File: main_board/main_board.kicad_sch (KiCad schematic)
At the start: 65 parts, among them J1 USB_B_Micro, J2 Conn_ARM_JTAG_SWD_10, Q1 NX3008PBK,215, Q2 T2N7002AK,LM, Q3 NX3008PBK,215, U1 SSD1306, U2 ESP32-S2-SOLO, U3 TLV62568PDRLT, U4 MCP73832, U7 MAX17055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

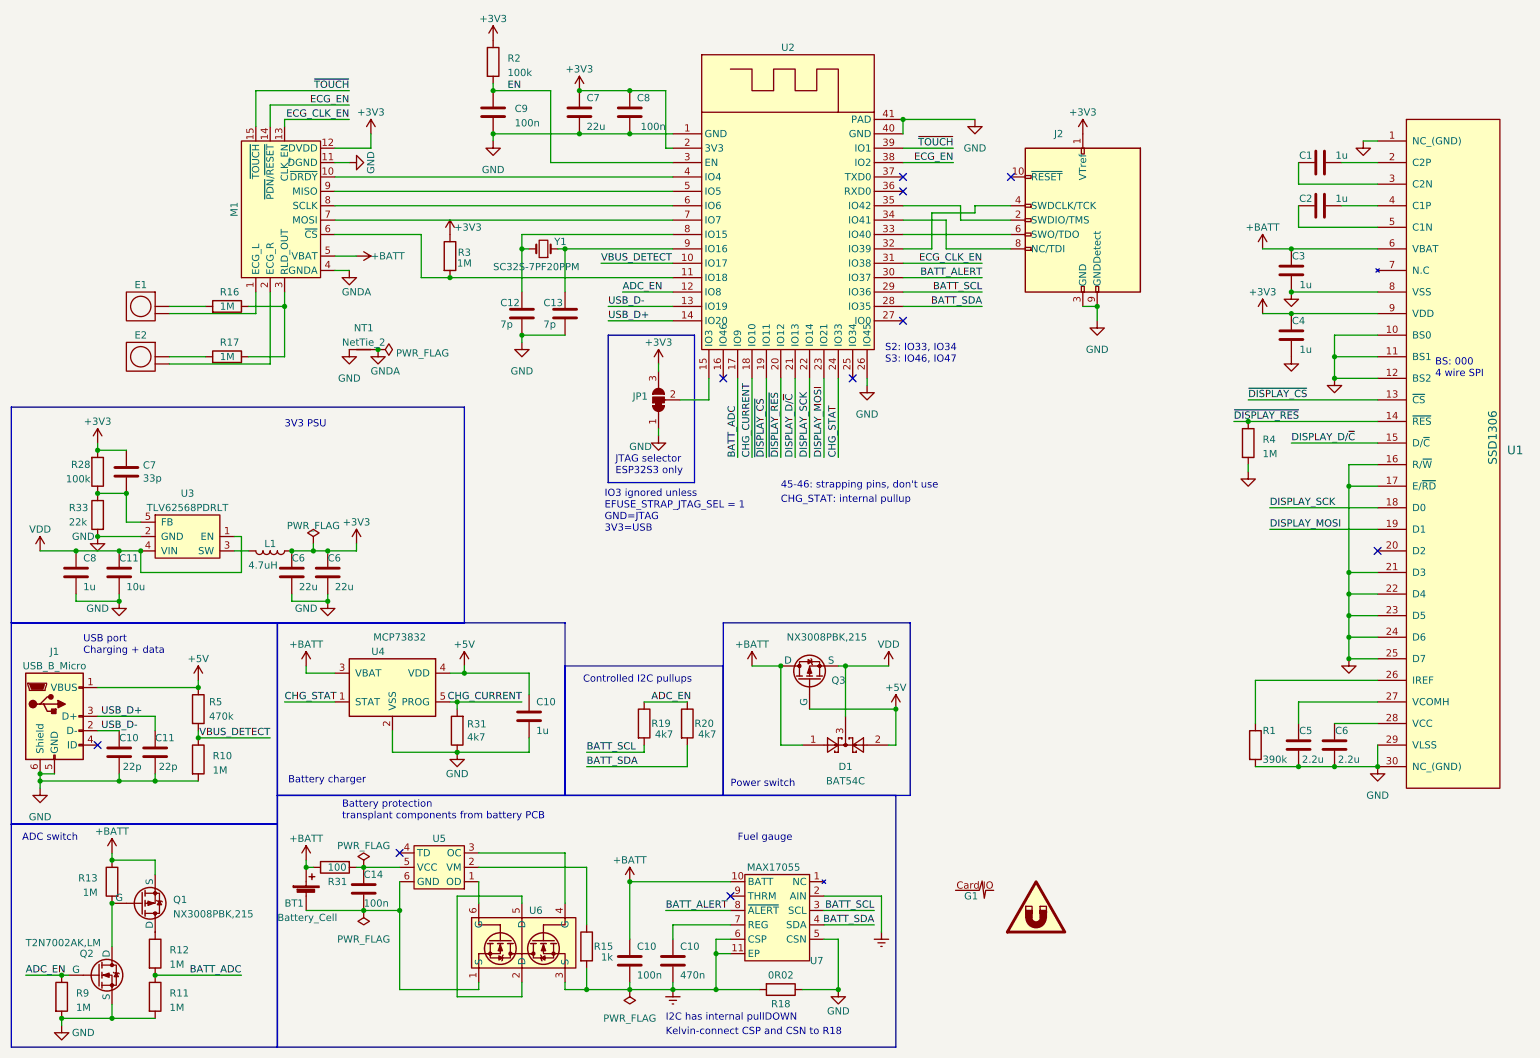
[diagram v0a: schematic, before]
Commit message: Remove battery ADC parts, simplify and tweak routing, add locking holes to jtag
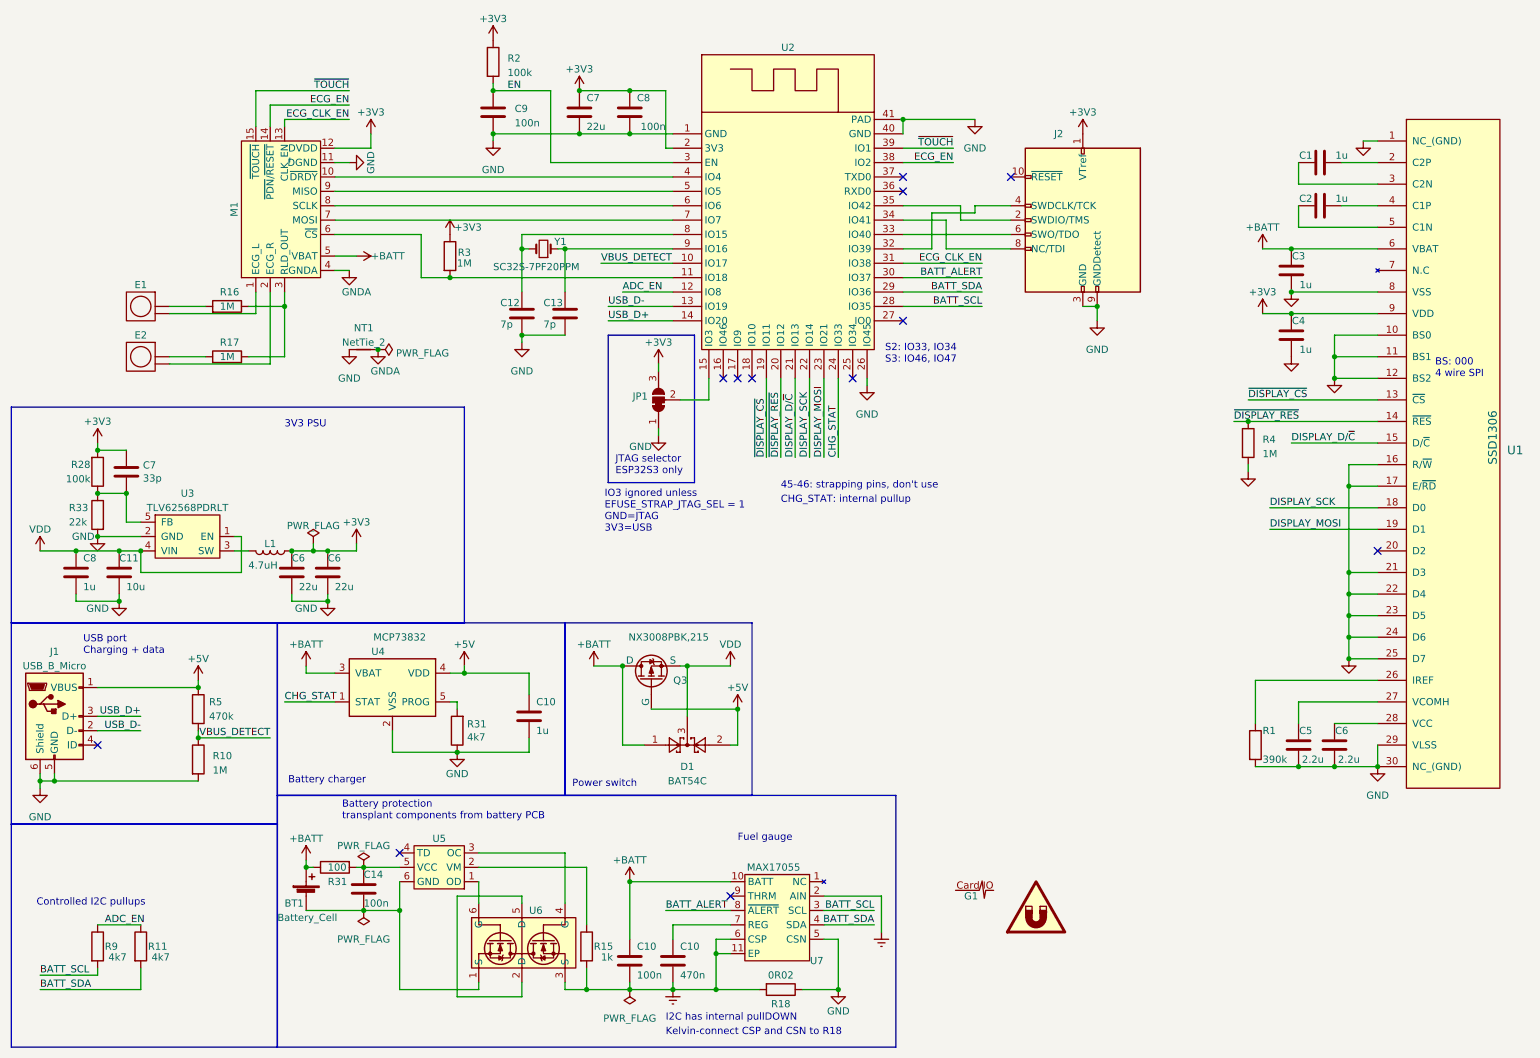
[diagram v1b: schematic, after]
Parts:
- removed C10, C11: 22p, Capacitor_SMD:C_0603_1608Metric, symbol Device:C
- removed Q1: NX3008PBK,215, Package_TO_SOT_SMD:SOT-23, symbol main_board_parts:PMOS
- removed Q2: T2N7002AK,LM, Package_TO_SOT_SMD:SOT-23, symbol main_board_parts:NMOS
- removed R12, R13: 1M, Resistor_SMD:R_0603_1608Metric, symbol Device:R
- removed R19, R20: 4k7, Resistor_SMD:R_0603_1608Metric, symbol Device:R
- R11, R9: value 1M -> 4k7
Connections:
- net ADC_EN: now also R11.1
- net BATT_SCL: now also R9.2, U2.28 (IO35); no longer U2.29 (IO36)
- net BATT_SDA: now also R11.2, U2.29 (IO36); no longer U2.28 (IO35)
- net GND: no longer R11.2, R9.2
- net BATT_ADC: no longer names the net of U2.17 (IO9)
- net BATT_ADC: no longer R11.1
- net CHG_CURRENT: no longer names the net of R31.2, U4.5 (PROG)
- net CHG_CURRENT: no longer U2.18 (IO10)
- no-connect marks 10 -> 12
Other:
- note removed: "ADC switch"
- moved on the sheet: D1, Q3

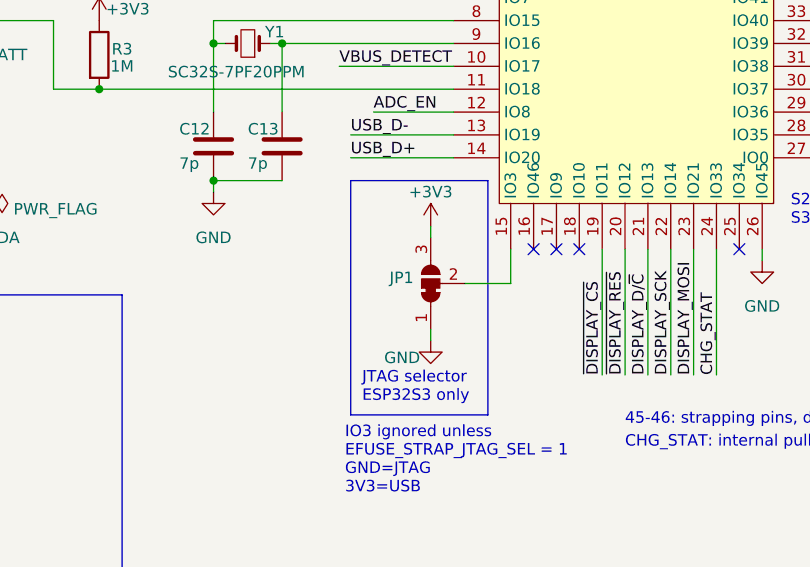
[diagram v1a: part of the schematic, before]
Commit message: Remove default link from jtag selector
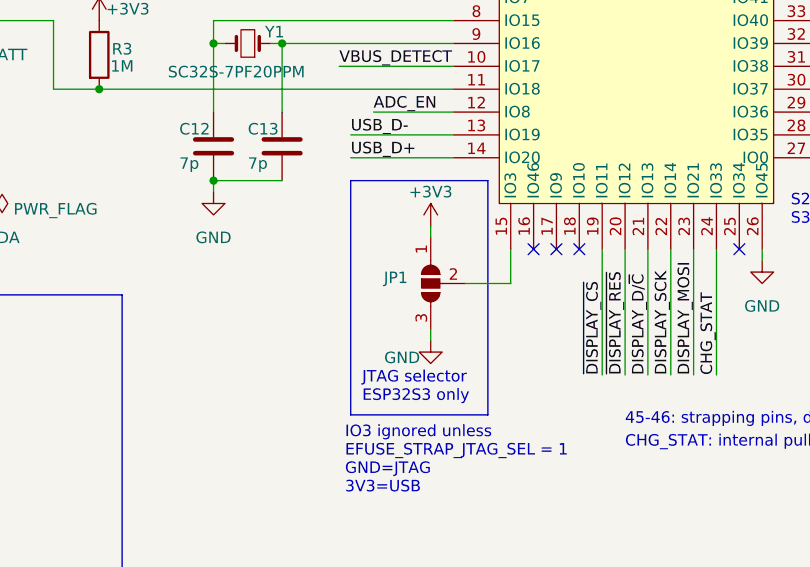
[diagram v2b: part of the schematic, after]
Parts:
- removed JP1: SolderJumper_3_Bridged12, Jumper:SolderJumper-3_P1.3mm_Bridged12_RoundedPad1.0x1.5mm, symbol Jumper:SolderJumper_3_Bridged12
- added JP1: SolderJumper_3_Open, Jumper:SolderJumper-3_P1.3mm_Open_RoundedPad1.0x1.5mm, symbol Jumper:SolderJumper_3_Open
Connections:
- net +3V3: now also JP1.1 (A)
- net GND: now also JP1.3 (B)
- net at U2.15 (IO3): now also JP1.2 (C)
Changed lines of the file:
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@@
-    )
-  )
-  (symbol (lib_id "Jumper:SolderJumper_3_Bridged12") (at 127 82.55 90) (unit 1)
-    (in_bom no) (on_board yes) (dnp no) (fields_autoplaced)
-    (property "Reference" "JP1" (at 125.095 81.915 90)
-      (effects (font (size 1.27 1.27)) (justify left))
-    )
-    (property "Value" "SolderJumper_3_Bridged12" (at 125.095 84.455 90)
-      (effects (font (size 1.27 1.27)) (justify left) hide)
-    )
-    (property "Footprint" "Jumper:SolderJumper-3_P1.3mm_Bridged12_RoundedPad1.0x1.5mm" (at 127 82.55 0)
-      (effects (font (size 1.27 1.27)) hide)
-    )
-    (property "Datasheet" "~" (at 127 82.55 0)
-      (effects (font (size 1.27 1.27)) hide)
-    )
-    (pin "1")
-    (pin "2")
-    (pin "3")
-    (instances
-      (project "main_board"
-        (path "/e55848cd-275a-4b5e-8e68-b5d8d07c8d31"
-          (reference "JP1") (unit 1)
-        )
-      )
     )
   )
@@
         )
       )
+    )
+  )
+  (symbol (lib_id "Jumper:SolderJumper_3_Open") (at 127 82.55 90) (mirror x) (unit 1)
+    (in_bom yes) (on_board yes) (dnp no)
+    (property "Reference" "JP1" (at 124.46 81.915 90)
+      (effects (font (size 1.27 1.27)) (justify left))
+    )
+    (property "Value" "SolderJumper_3_Open" (at 124.46 80.645 90)
+      (effects (font (size 1.27 1.27)) (justify left) hide)
+    )
+    (property "Footprint" "Jumper:SolderJumper-3_P1.3mm_Open_RoundedPad1.0x1.5mm" (at 127 82.55 0)
+      (effects (font (size 1.27 1.27)) hide)
+    )
+    (property "Datasheet" "~" (at 127 82.55 0)
+      (effects (font (size 1.27 1.27)) hide)
+    )
+    (pin "1")
+    (pin "2")
+    (pin "3")
+    (instances
+      (project "main_board"
+        (path "/e55848cd-275a-4b5e-8e68-b5d8d07c8d31"
+          (reference "JP1") (unit 1)
+        )
+      )

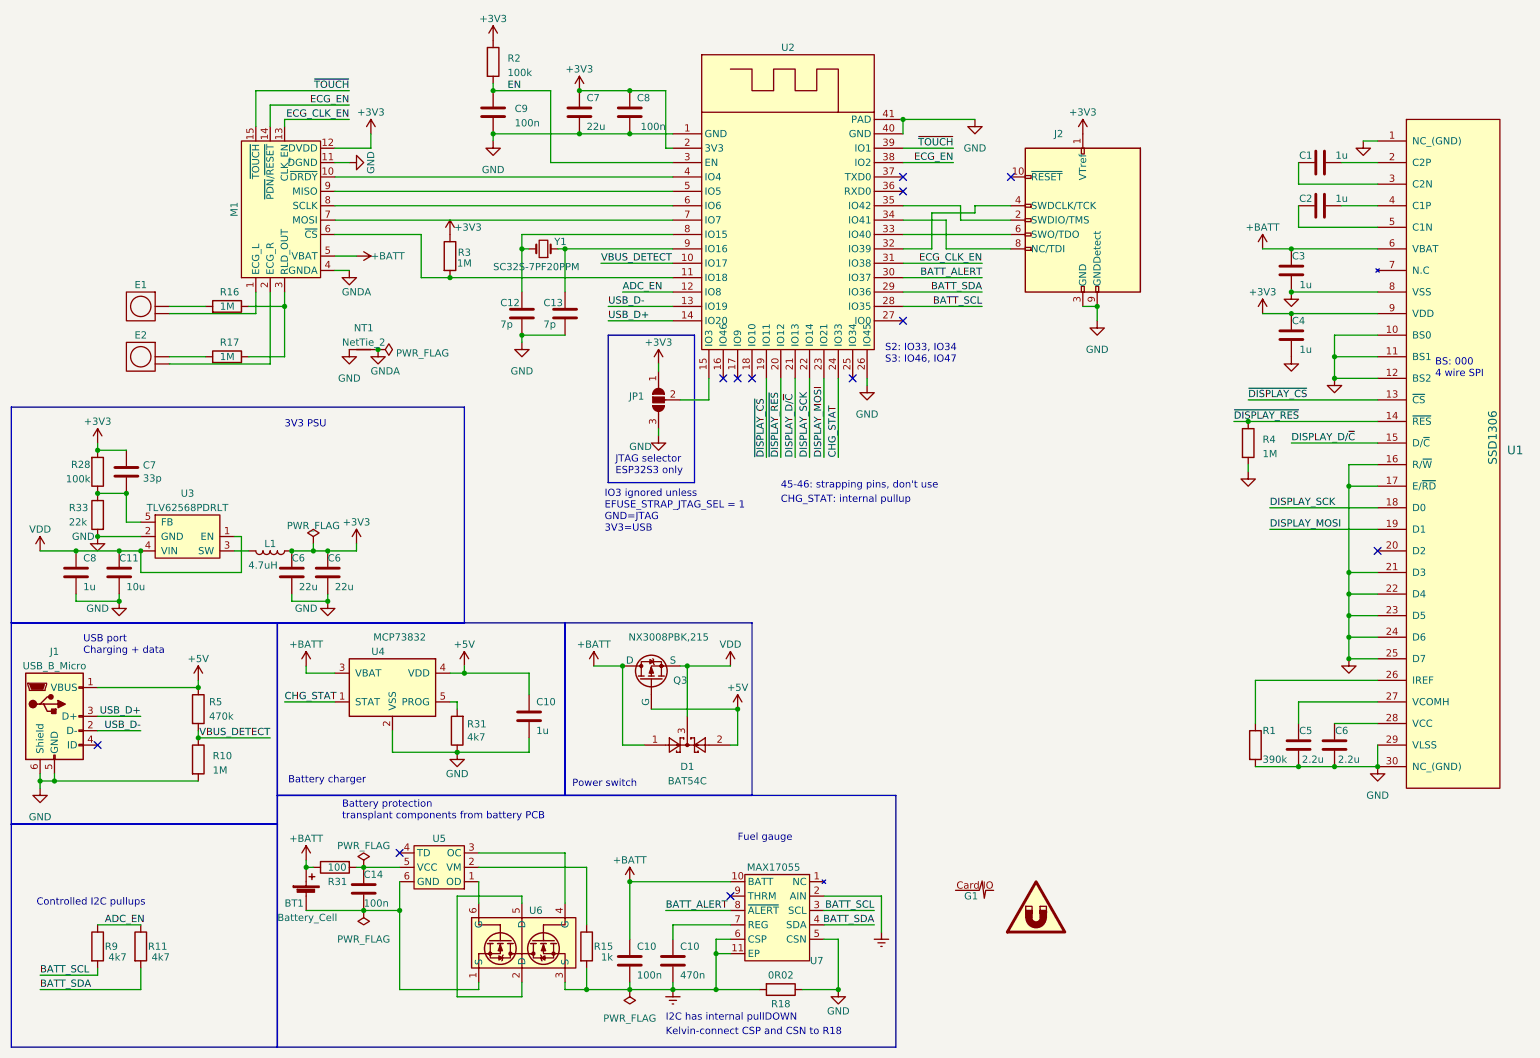
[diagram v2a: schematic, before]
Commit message: Replace USB with USB4105-GF-A-060
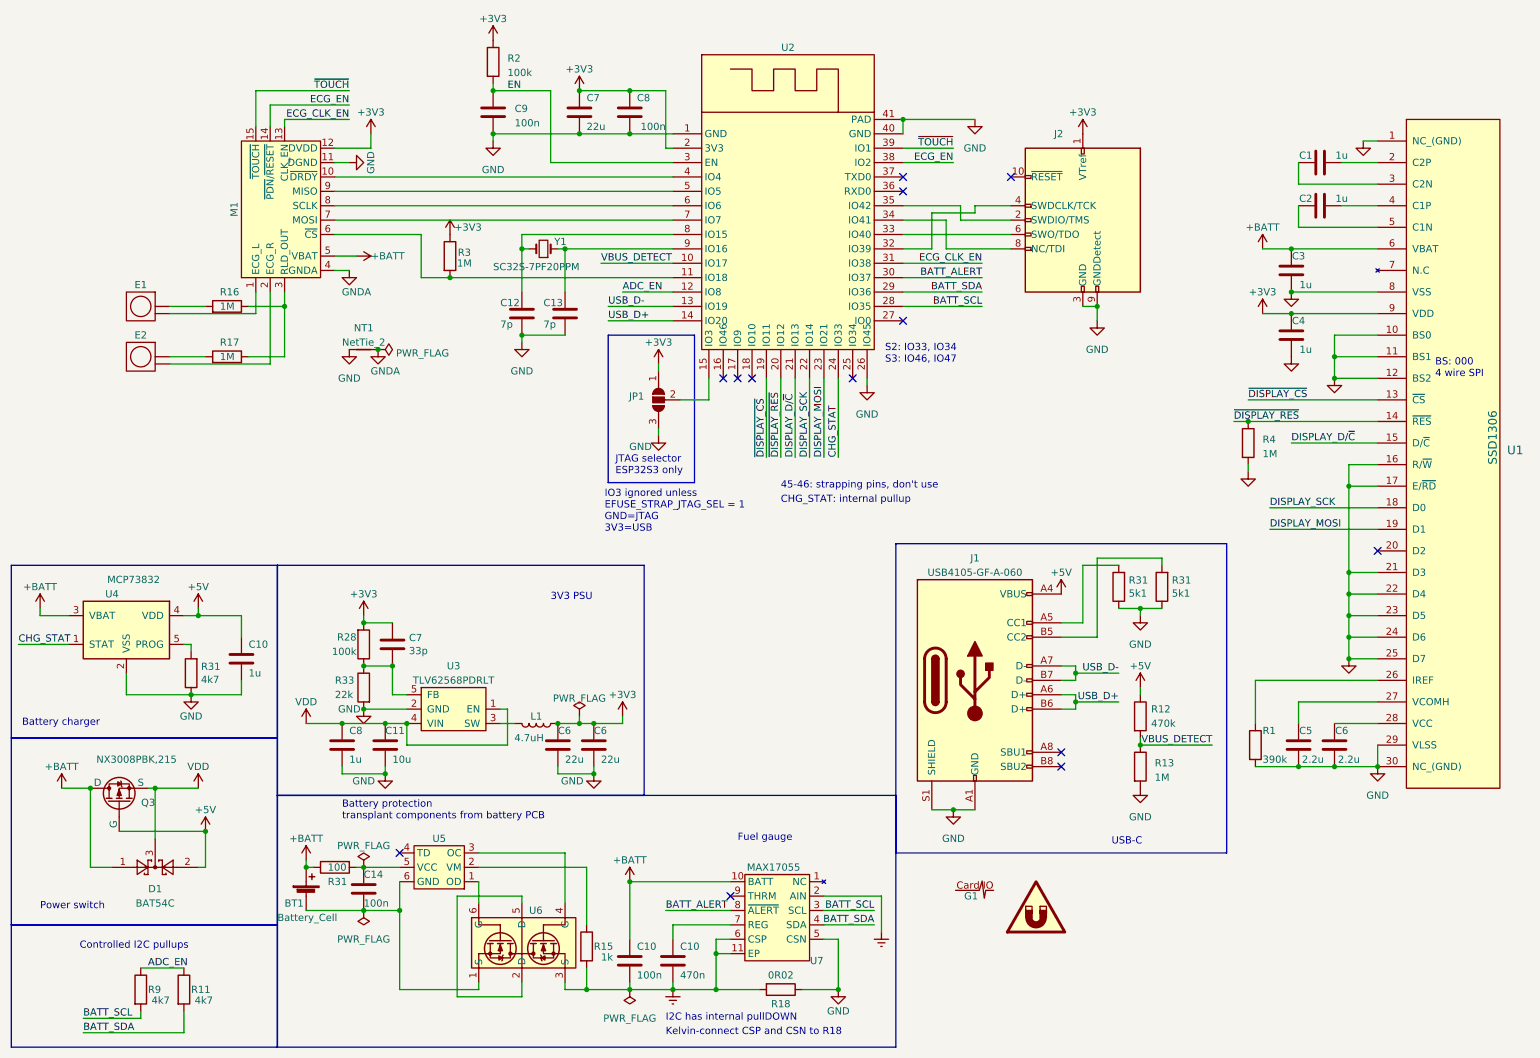
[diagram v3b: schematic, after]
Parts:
- removed J1: USB_B_Micro, main_board_parts:USB_Micro-B_Molex-47642-0001, symbol Connector:USB_B_Micro
- removed R10: 1M, Resistor_SMD:R_0603_1608Metric, symbol Device:R
- removed R5: 470k, Resistor_SMD:R_0603_1608Metric, symbol Device:R
- added J1: USB4105-GF-A-060, Connector_USB:USB_C_Receptacle_GCT_USB4105-xx-A_16P_TopMnt_Horizontal, symbol Connector:USB_C_Receptacle_USB2.0
- added R12: 470k, Resistor_SMD:R_0603_1608Metric, symbol Device:R
- added R13: 1M, Resistor_SMD:R_0603_1608Metric, symbol Device:R
- added R31 (x2): 5k1, Resistor_SMD:R_0603_1608Metric, symbol Device:R
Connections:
- net +5V: now also J1.A4 (VBUS), J1.A9 (VBUS), J1.B4 (VBUS), J1.B9 (VBUS), R12.1
- net GND: now also J1.A1 (GND), J1.A12 (GND), J1.B1 (GND), J1.B12 (GND), J1.S1 (SHIELD), R13.2, R31.1, R31.1
- net USB_D+: now also J1.A6 (D+), J1.B6 (D+)
- net USB_D-: now also J1.A7 (D-), J1.B7 (D-)
- net VBUS_DETECT: now also R12.2, R13.1
- new net: J1.A5 (CC1), R31.2
- new net: J1.B5 (CC2), R31.2
- no-connect marks 12 -> 13
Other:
- note added: "USB-C"
- note removed: "USB port Charging + data"
- moved on the sheet: C10, C11, C6, C7, C8, D1, L1, Q3, R11, R28, R31, R33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

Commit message: Finalize v1r4
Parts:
- R11, R31, R9: value 4k7 -> 5k1
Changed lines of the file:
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@@
   (title_block
     (title "Card/IO ECG main board")
-    (date "2023-07-19")
+    (date "2023-08-24")
     (rev "4")
   )
@@
       (effects (font (size 1.27 1.27)) (justify right))
     )
-    (property "Value" "4k7" (at 46.2026 131.953 0)
+    (property "Value" "5k1" (at 46.2026 131.953 0)
       (effects (font (size 1.27 1.27)) (justify right))
     )
@@
       (effects (font (size 1.27 1.27)) (justify left))
     )
-    (property "Value" "4k7" (at 45.085 188.595 0)
+    (property "Value" "5k1" (at 45.085 188.595 0)
       (effects (font (size 1.27 1.27)) (justify left))
     )
@@
       (effects (font (size 1.27 1.27)) (justify left))
     )
-    (property "Value" "4k7" (at 37.465 188.595 0)
+    (property "Value" "5k1" (at 37.465 188.595 0)
       (effects (font (size 1.27 1.27)) (justify left))
     )
